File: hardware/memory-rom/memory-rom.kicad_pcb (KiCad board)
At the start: 2 copper layers, 77 x 39 mm, 27 parts, among them J1 Conn_Mem_Ext, J2 Conn_Power, U1 SST39VF040-70-4C-NHE, U2 74LVC1G86, U3 74LVC1G32, U4 74LVC1G332, U5 74LVC1G86, U6 MIC5504-3.3YM5

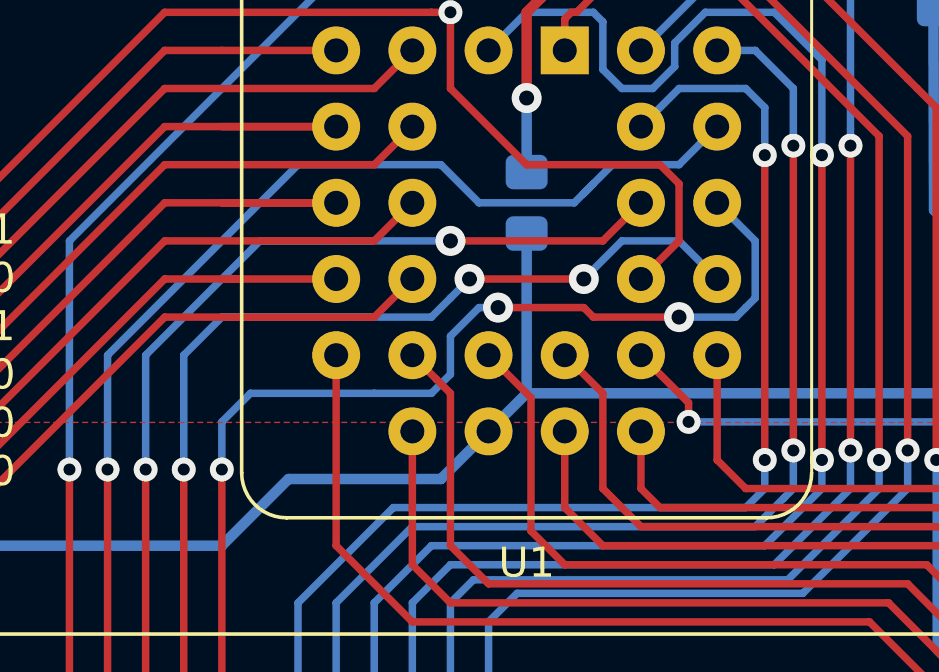
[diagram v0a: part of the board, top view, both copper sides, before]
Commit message: Rev B of memory-rom: switch OE and CE
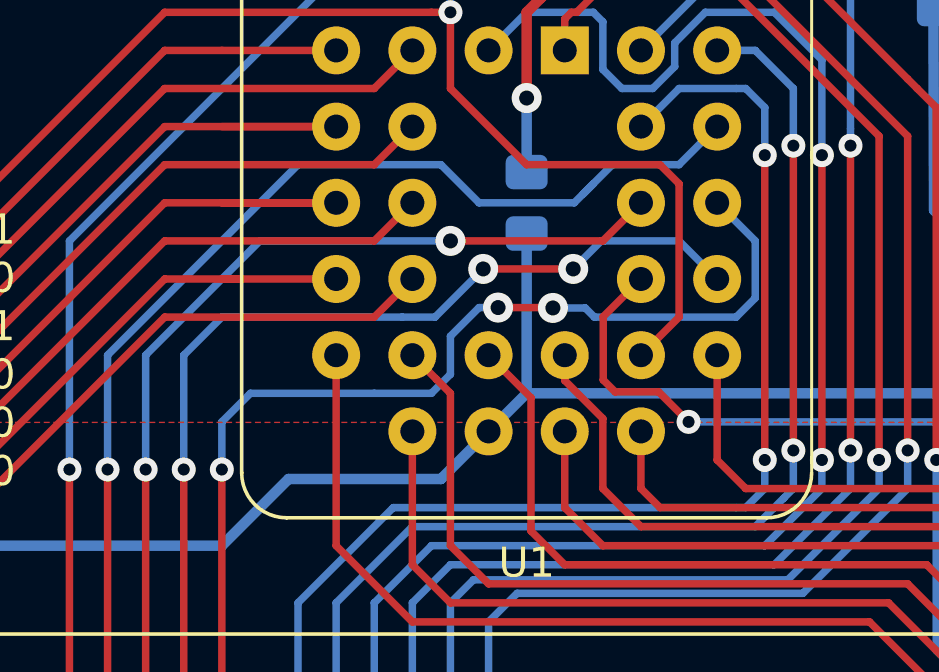
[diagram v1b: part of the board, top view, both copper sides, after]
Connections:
- U1 pad 22: /~MEM_OE -> /~CE
- U1 pad 24: /~CE -> /~MEM_OE
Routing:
- net /~MEM_OE: track 35.7 -> 40.1 mm
- net /~CE: track 78.8 -> 81.4 mm
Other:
- board text added: "Rev B 2022-01-22"
- board text removed: "2020-06-11"

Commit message: Add revision number to the front silk screen
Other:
- rule pad_to_mask_clearance: 0.051 -> 0
- board text added: "2022-01-22"
- board text added: "Rev B"
- board text removed: "Rev B 2022-01-22"

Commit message: Update all to Kicad 6
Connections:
- net /~CE renamed /~{CE}
- net /~MEM_OE renamed /~{MEM_OE}
- net /~MEM_WE renamed /~{MEM_WE}
- net /~RESET renamed /~{RESET}
- net /~WAIT renamed /~{WAIT}
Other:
- net class Default removed
